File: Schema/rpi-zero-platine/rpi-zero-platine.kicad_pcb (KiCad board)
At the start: 2 copper layers, 115.2 x 38.2 mm, 4 parts, among them J1 GPIO, J2 Screw_Terminal_01x06, J3 Screw_Terminal_01x02, SW1 SW_DIP_x02

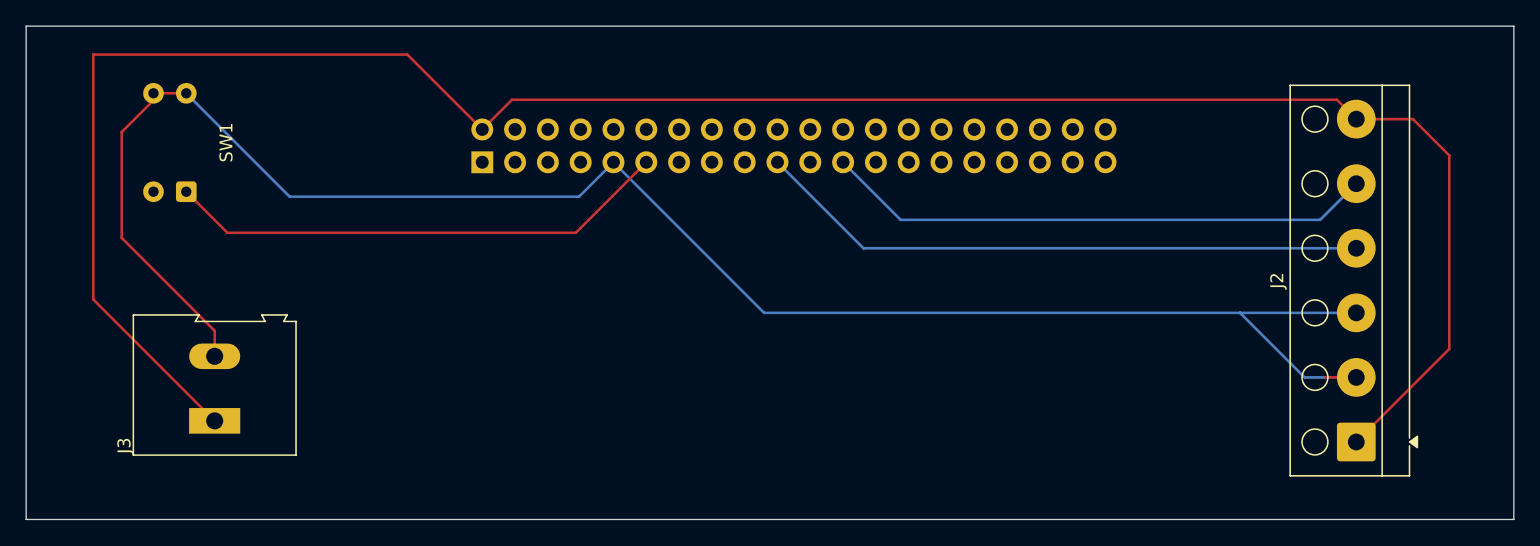
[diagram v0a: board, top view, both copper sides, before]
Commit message: Ändere Footprint der Schraubklemmen auf Phoenix mit 3D-Model
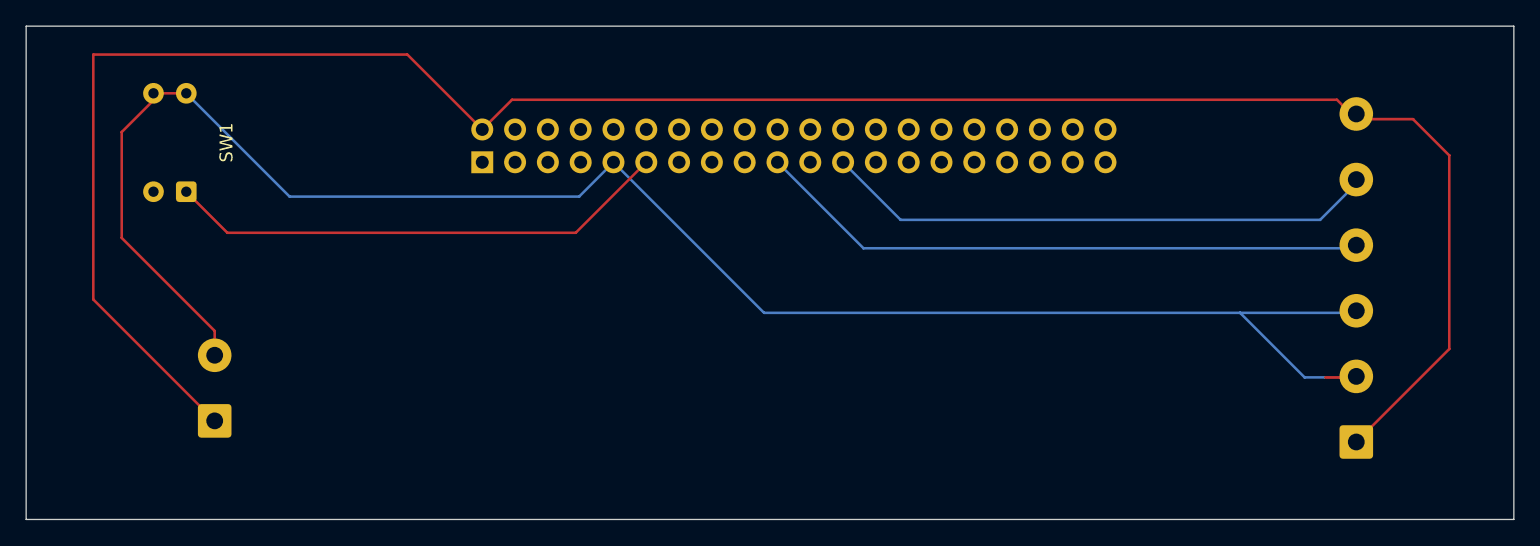
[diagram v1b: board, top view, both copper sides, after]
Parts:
- J2: footprint TerminalBlock_Altech:Altech_AK100_1x06_P5.00mm -> TerminalBlock_Phoenix:TerminalBlock_Phoenix_MKDS-1,5-6-5.08_1x06_P5.08mm_Horizontal; moved to B.Cu
- J3: footprint TerminalBlock:TerminalBlock_Altech_AK300-2_P5.00mm -> TerminalBlock_Phoenix:TerminalBlock_Phoenix_MKDS-1,5-2-5.08_1x02_P5.08mm_Horizontal; moved to B.Cu

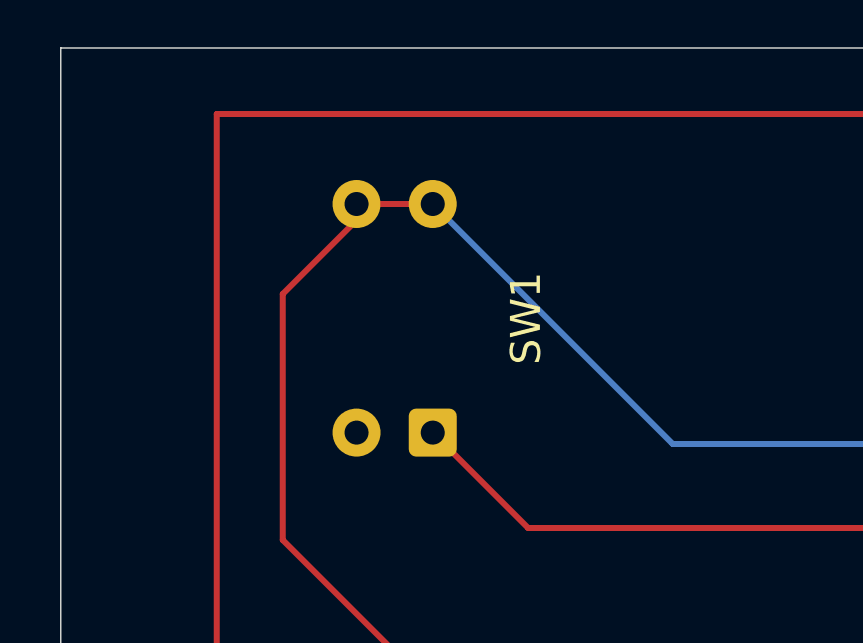
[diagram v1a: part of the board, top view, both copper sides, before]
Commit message: Ändere Footprint des Switches
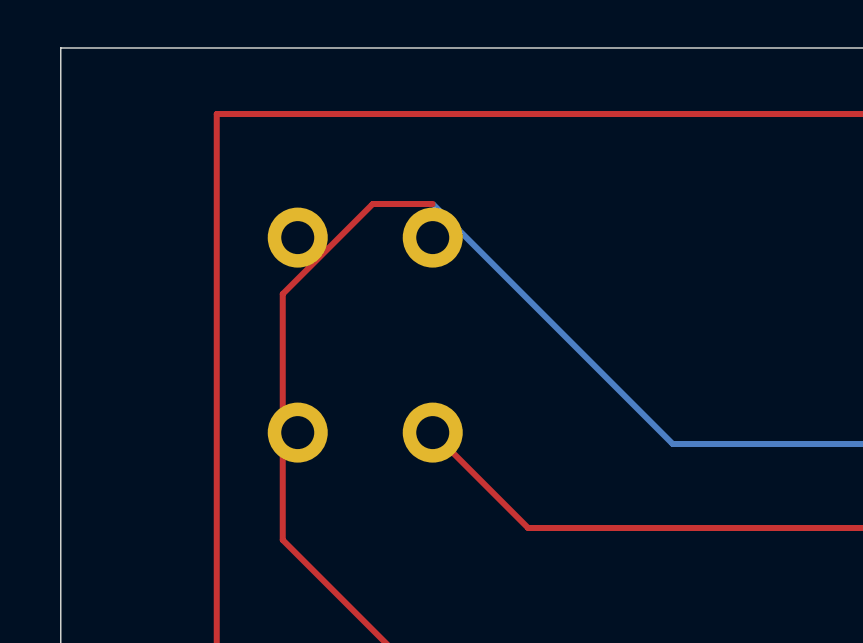
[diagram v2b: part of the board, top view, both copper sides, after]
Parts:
- SW1: footprint Button_Switch_THT:SW_DIP_SPSTx02_Piano_10.8x6.64mm_W7.62mm_P2.54mm -> Button_Switch_THT:SW_PUSH_6mm_H4.3mm

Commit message: Überarbeite Platine
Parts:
- J1: footprint Connector_PinSocket_2.54mm:PinSocket_2x20_P2.54mm_Vertical -> Connector_PinSocket_2.54mm:PinSocket_2x13_P2.54mm_Vertical; moved to F.Cu
- J2, J3, SW1: moved to F.Cu
- moved J3 22.8 mm to (89.2, 73.2), turned to -90 degrees
- moved SW1 18.4 mm to (92.2, 96.1), turned to 180 degrees
- moved J1 16.0 mm to (108.8, 91.8), turned to 90 degrees
- moved J2 0.45 mm to (178.4, 98.0)
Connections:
- J1 pad 1: +3V3 -> unconnected-(J1-Pin_1-Pad1)
- J1 pad 10: /GPIO15/RXD0 -> unconnected-(J1-Pin_10-Pad10)
- J1 pad 11: /GPIO17 -> unconnected-(J1-BU-Pad11)
- J1 pad 12: /GPIO18/PCM.CLK -> unconnected-(J1-Pin_12-Pad12)
- J1 pad 13: /GPIO27 -> unconnected-(J1-Pin_13-Pad13)
- J1 pad 14: GND -> unconnected-(J1-Pin_14-Pad14)
- J1 pad 15: /GPIO22 -> Net-(J1-Pin_15)
- J1 pad 16: /GPIO23 -> unconnected-(J1-Pin_16-Pad16)
- J1 pad 17: +3V3 -> unconnected-(J1-Pin_17-Pad17)
- J1 pad 18: /GPIO24 -> unconnected-(J1-Pin_18-Pad18)
- J1 pad 19: /GPIO10/SPI0.MOSI -> Net-(J1-SPI0.MOSI)
- J1 pad 20: GND -> unconnected-(J1-Pin_20-Pad20)
- J1 pad 21: /GPIO9/SPI0.MISO -> unconnected-(J1-Pin_21-Pad21)
- J1 pad 22: /GPIO25 -> unconnected-(J1-Pin_22-Pad22)
- J1 pad 23: /GPIO11/SPI0.SCLK -> Net-(J1-SPI0.SCLK)
- J1 pad 24: /GPIO8/SPI0.CE0 -> unconnected-(J1-Pin_24-Pad24)
- J1 pad 26: /GPIO7/SPI0.CE1 -> unconnected-(J1-Pin_26-Pad26)
- J1 pad 3: /GPIO2/SDA1 -> unconnected-(J1-Pin_3-Pad3)
- J1 pad 4: +5V -> unconnected-(J1-Pin_4-Pad4)
- J1 pad 5: /GPIO3/SCL1 -> unconnected-(J1-Pin_5-Pad5)
- J1 pad 6: GND -> unconnected-(J1-Pin_6-Pad6)
- J1 pad 7: /GPIO4/GPCLK0 -> unconnected-(J1-Pin_7-Pad7)
- J1 pad 8: /GPIO14/TXD0 -> unconnected-(J1-Pin_8-Pad8)
- J1 pad 9: GND -> Net-(J1-Pin_9)
- J2 pad 4: /GPIO10/SPI0.MOSI -> Net-(J1-SPI0.SCLK)
- J2 pad 5: /GPIO11/SPI0.SCLK -> Net-(J1-SPI0.MOSI)
- J3 pad 1: +5V -> GND
- J3 pad 2: GND -> +5V
- SW1 pad 1: /GPIO17 -> Net-(J1-Pin_9)
- SW1 pad 2: unconnected-(SW1-Pad2) -> Net-(J1-Pin_15)
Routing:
- net Net-(J1-SPI0.MOSI): track 0.00 -> 52.5 mm
- net /GPIO10/SPI0.MOSI: track 47.6 -> 0.00 mm
- net Net-(J1-SPI0.SCLK): track 0.00 -> 45.5 mm
- net /GPIO11/SPI0.SCLK: track 42.7 -> 0.00 mm
- net /GPIO17: track 39.2 -> 0.00 mm
- net Net-(J1-Pin_15): track 0.00 -> 38.5 mm
- net GND: track 139.9 -> 102.4 mm
- net +5V: track 167.6 -> 133.5 mm
- net Net-(J1-Pin_9): track 0.00 -> 31.4 mm

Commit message: Beschriftung
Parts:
- J2: value Screw_Terminal_01x06 -> LED Out A
- J3: value Screw_Terminal_01x02 -> LED Out B
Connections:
- net Net-(J1-SPI0.MOSI) renamed /Data
- net Net-(J1-SPI0.SCLK) renamed /Clock
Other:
- board text added: "C"
- board text added: "D"
- board text added: "GND"
- board text added: "V+"
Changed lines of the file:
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@@
 	(net 21 "unconnected-(J1-Pin_26-Pad26)")
 	(net 22 "unconnected-(J1-Pin_5-Pad5)")
-	(net 23 "Net-(J1-SPI0.SCLK)")
+	(net 23 "/Clock")
 	(net 24 "Net-(J1-Pin_15)")
-	(net 25 "Net-(J1-SPI0.MOSI)")
+	(net 25 "/Data")
 	(net 26 "Net-(J1-Pin_9)")
 	(footprint "Connector_PinSocket_2.54mm:PinSocket_2x13_P2.54mm_Vertical"
@@
 			(layers "*.Cu" "*.Mask")
 			(remove_unused_layers no)
-			(net 25 "Net-(J1-SPI0.MOSI)")
+			(net 25 "/Data")
 			(pinfunction "SPI0.MOSI")
 			(pintype "passive")
@@
 			(layers "*.Cu" "*.Mask")
 			(remove_unused_layers no)
-			(net 23 "Net-(J1-SPI0.SCLK)")
+			(net 23 "/Clock")
 			(pinfunction "SPI0.SCLK")
 			(pintype "passive")
@@
 			)
 		)
-		(property "Value" "Screw_Terminal_01x02"
+		(property "Value" "LED Out B"
 			(at 2.54 5.72 90)
 			(layer "F.Fab")
@@
 			(roundrect_rratio 0.096154)
 			(net 1 "GND")
-			(pinfunction "Pin_1")
-			(pintype "passive")
+			(pinfunction "LEDB-")
+			(pintype "power_out")
 		)
 		(pad "2" thru_hole circle
@@
 			(remove_unused_layers no)
 			(net 2 "+5V")
-			(pinfunction "Pin_2")
-			(pintype "passive")
+			(pinfunction "LEDB+")
+			(pintype "power_out")
 		)
 		(embedded_fonts no)
@@
 			)
 		)
-		(property "Value" "Screw_Terminal_01x06"
+		(property "Value" "LED Out A"
 			(at 12.7 5.72 90)
 			(layer "F.Fab")
@@
 			(layers "*.Cu" "*.Mask")
 			(remove_unused_layers no)
-			(net 23 "Net-(J1-SPI0.SCLK)")
+			(net 23 "/Clock")
 			(pinfunction "Pin_4")
 			(pintype "passive")
@@
 			(layers "*.Cu" "*.Mask")
 			(remove_unused_layers no)
-			(net 25 "Net-(J1-SPI0.MOSI)")
+			(net 25 "/Data")
 			(pinfunction "Pin_5")
 			(pintype "passive")
@@
 		(layer "Dwgs.User")
 	)
-	(gr_line
-		(start 100 73)
-		(end 100 72.5)
-		(stroke
-			(width 0.1)
-			(type solid)
-		)
-		(layer "Dwgs.User")
-	)
 	(gr_rect
 		(start 75.6 65.4)
@@
 		(layer "Edge.Cuts")
 	)
+	(gr_text "C"
+		(at 187 83.8 90)
+		(layer "F.SilkS")
+		(effects
+			(font
+				(size 1 1)
+				(thickness 0.15)
+			)
+			(justify left bottom)
+		)
+	)
+	(gr_text "GND"
+		(at 187 89.4 90)
+		(layer "F.SilkS")
+		(effects
+			(font
+				(size 1 1)
+				(thickness 0.15)
+			)
+			(justify left bottom)
+		)
+	)
+	(gr_text "GND"
+		(at 80.4 71.4 270)
+		(layer "F.SilkS")
+		(effects
+			(font
+				(size 1 1)
+				(thickness 0.15)
+			)
+			(justify left bottom)
+		)
+	)
+	(gr_text "D"
+		(at 187.2 78.8 90)
+		(layer "F.SilkS")
+		(effects
+			(font
+				(size 1 1)
+				(thickness 0.15)
+			)
+			(justify left bottom)
+		)
+	)
+	(gr_text "V+"
+		(at 80.2 77.4 270)
+		(layer "F.SilkS")
+		(effects
+			(font
+				(size 1 1)
+				(thickness 0.15)
+			)
+			(justify left bottom)
+		)
+	)
+	(gr_text "V+"
+		(at 187.4 73.4 90)
+		(layer "F.SilkS")
+		(effects
+			(font
+				(size 1 1)
+				(thickness 0.15)
+			)
+			(justify left bottom)
+		)
+	)
+	(gr_text "V+"
+		(at 186.8 98.44 90)
+		(layer "F.SilkS")
+		(effects
+			(font
+				(size 1 1)
+				(thickness 0.15)
+			)
+			(justify left bottom)
+		)
+	)
+	(gr_text "GND"
+		(at 186.8 94 90)
+		(layer "F.SilkS")
+		(effects
+			(font
+				(size 1 1)
+				(thickness 0.15)
+			)
+			(justify left bottom)
+		)
+	)
 	(segment
